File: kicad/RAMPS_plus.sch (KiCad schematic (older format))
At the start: 20 parts, among them CON1 CON10, CON2 CON8, CON3 CON8, CON4 CON8, CON5 CON6, CON6 CON8, CON7 CON8, CON8 CON18x2

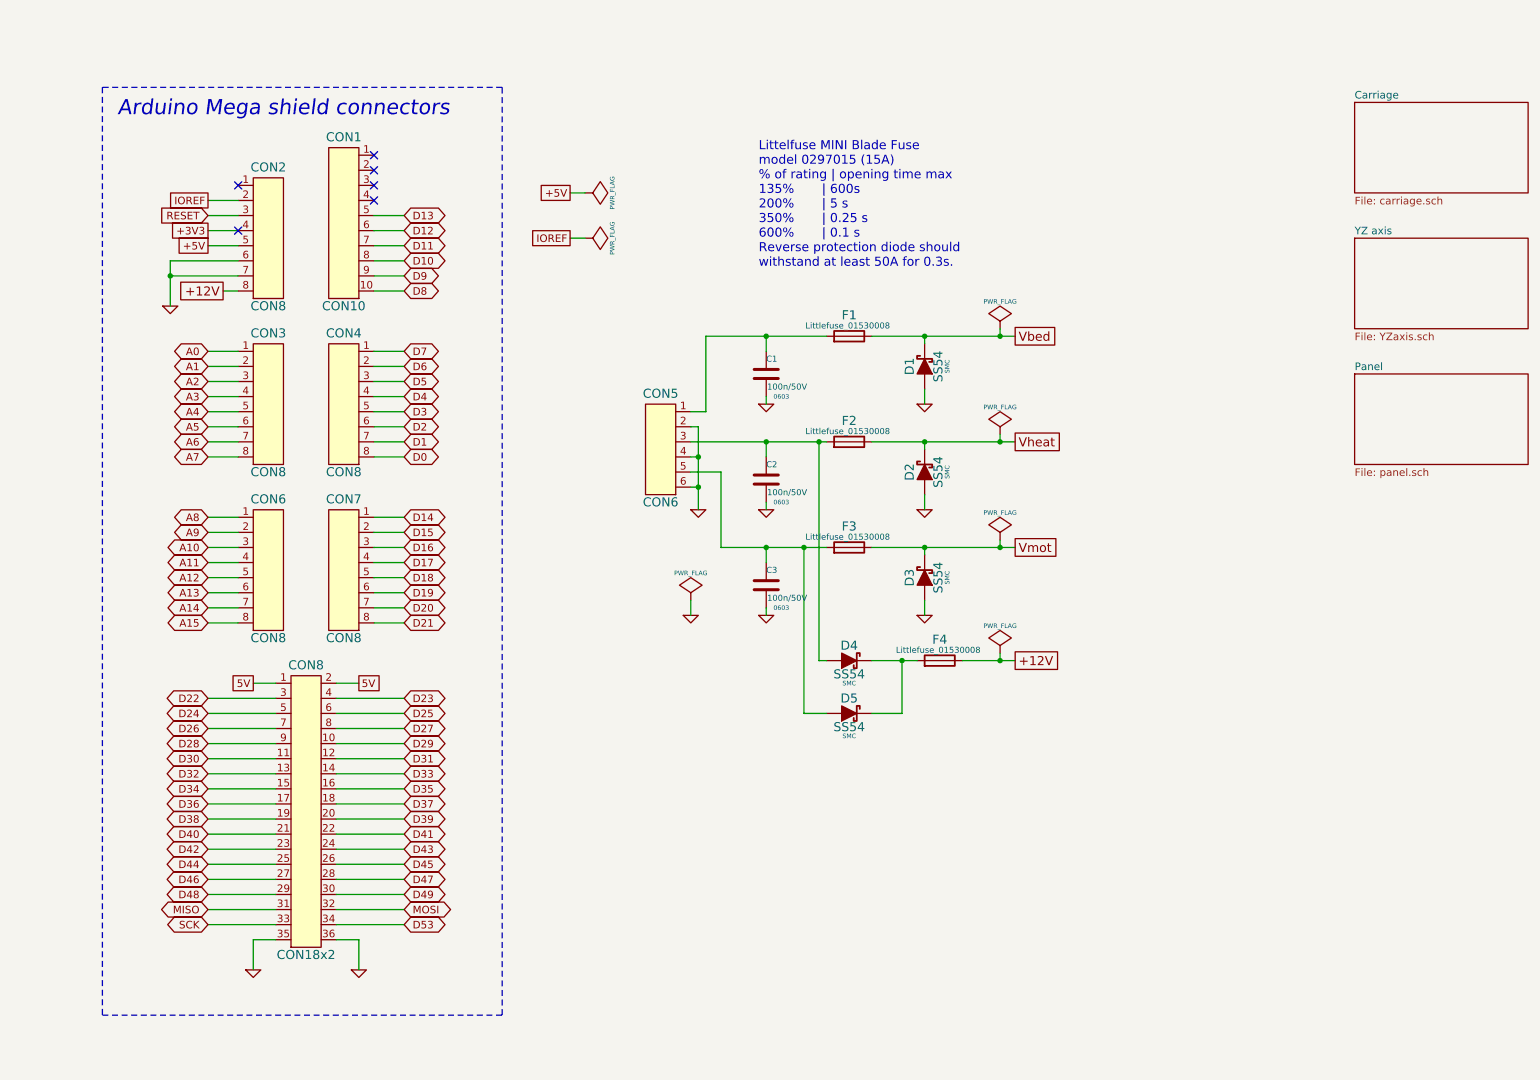
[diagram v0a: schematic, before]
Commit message: Change ULN2803 to discrete MOSFET's FDC6401N
Close #7
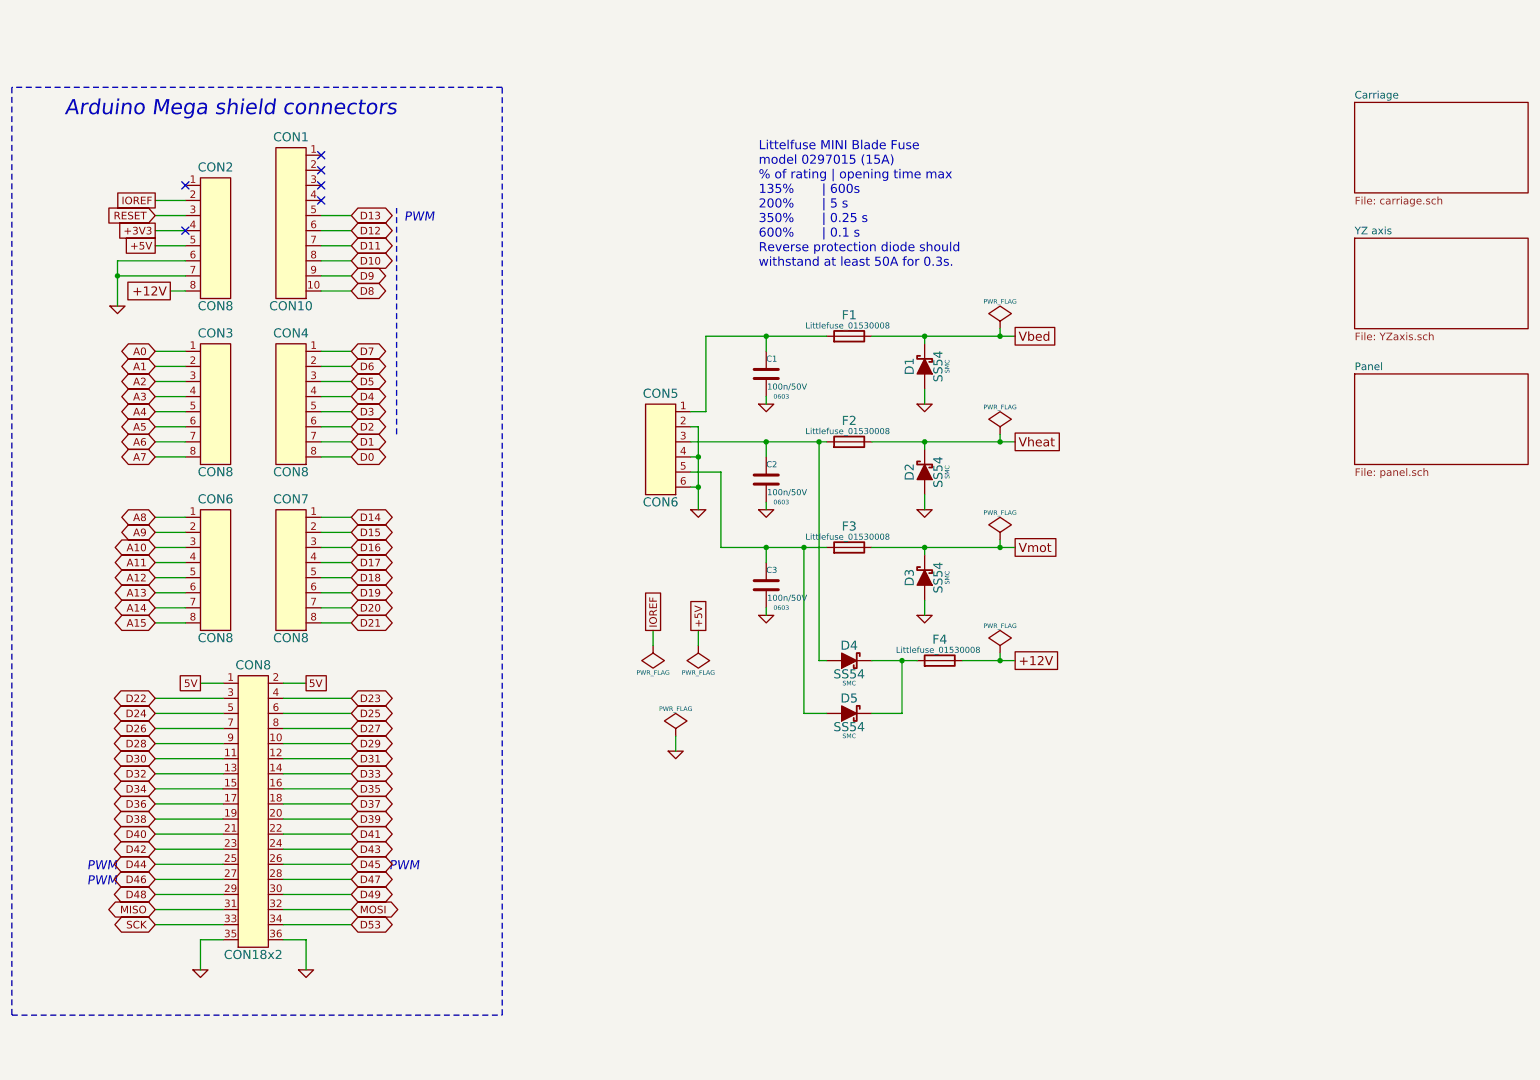
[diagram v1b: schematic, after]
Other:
- note added: "PWM"
- moved on the sheet: CON1, CON2, CON3, CON4, CON6, CON7, CON8

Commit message: Extract power supply circuits to another sheet. Add power off circuit.
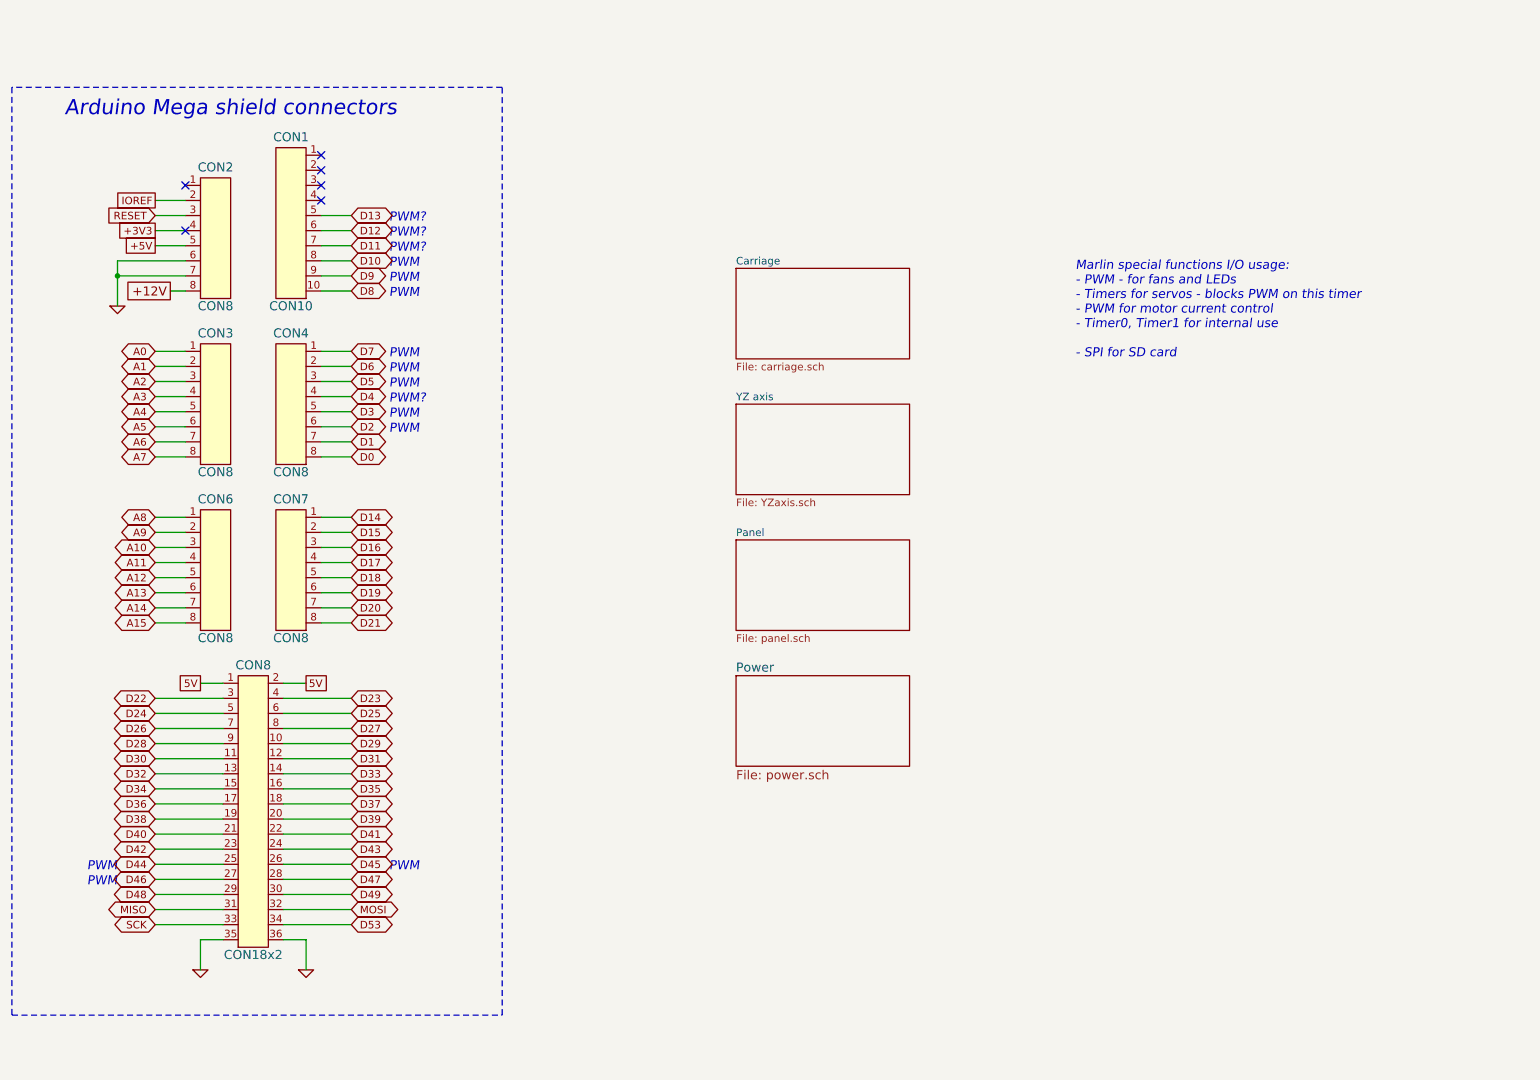
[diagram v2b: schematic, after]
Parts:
- removed C1, C2, C3: 100n/50V, 0603, symbol C
- removed CON5: CON6, symbol CON6
- removed D1, D2, D3, D4, D5: SS54, SMC, symbol SS54
- removed F1, F2, F3, F4: MINI_Blade_Fuse_Holder, Littlefuse_01530008, symbol MINI_Blade_Fuse_Holder
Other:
- note added: "Marlin special functions I/O usage:\n- PWM - for fans and LEDs\n- Timers for servos - blocks PWM on this timer\n- PWM for motor current control\n- Timer0, Timer1 for internal use\n\n- SPI for SD card"
- note added: "PWM?"
- note removed: "Littelfuse MINI Blade Fuse\nmodel 0297015 (15A)\n% of rating | opening time max\n135% | 600s\n200% | 5 s \n350% | 0.25 s \n600% | 0.1 s\nReverse protection diode should \nwithstand at least 50A for 0.3s."

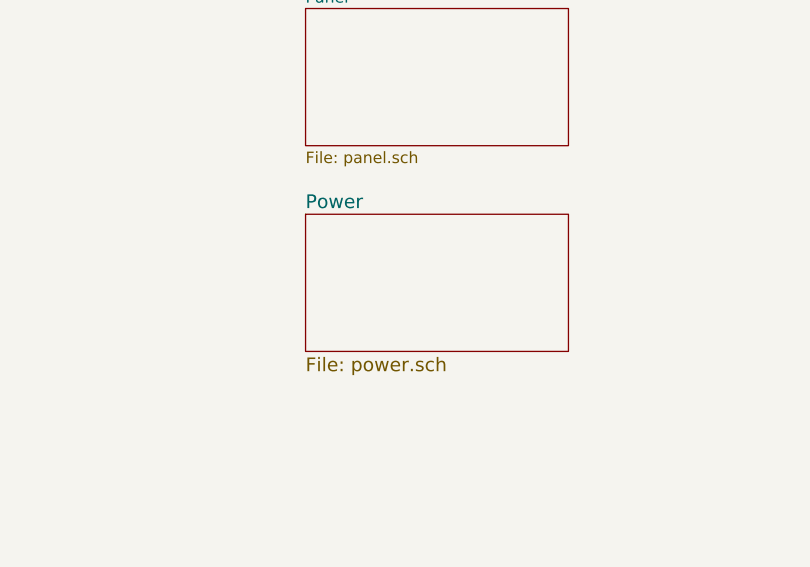
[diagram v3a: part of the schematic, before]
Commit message: Added fan connectors for electronics and power supply
close #15
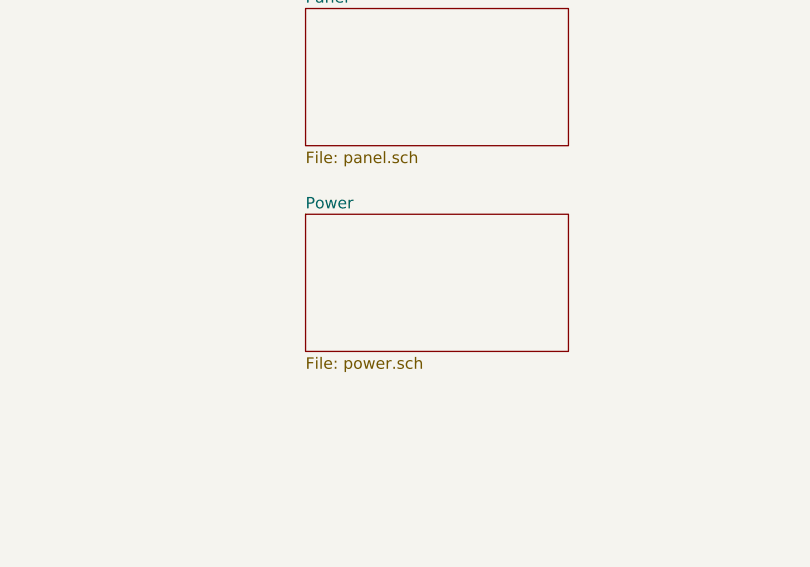
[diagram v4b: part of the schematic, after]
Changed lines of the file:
@@
 $EndComp
 $Comp
-L GND #PWR1
+L GND #PWR01
 U 1 1 536FA4F6
 P 1300 2500
-F 0 "#PWR1" H 1300 2500 30  0001 C CNN
+F 0 "#PWR01" H 1300 2500 30  0001 C CNN
 F 1 "GND" H 1300 2430 30  0001 C CNN
 F 2 "" H 1300 2500 60  0000 C CNN
@@
 $EndComp
 $Comp
-L GND #PWR3
+L GND #PWR02
 U 1 1 536FA739
 P 2550 6900
-F 0 "#PWR3" H 2550 6900 30  0001 C CNN
+F 0 "#PWR02" H 2550 6900 30  0001 C CNN
 F 1 "GND" H 2550 6830 30  0001 C CNN
 F 2 "" H 2550 6900 60  0000 C CNN
@@
 $EndComp
 $Comp
-L GND #PWR2
+L GND #PWR03
 U 1 1 536FA866
 P 1850 6900
-F 0 "#PWR2" H 1850 6900 30  0001 C CNN
+F 0 "#PWR03" H 1850 6900 30  0001 C CNN
 F 1 "GND" H 1850 6830 30  0001 C CNN
 F 2 "" H 1850 6900 60  0000 C CNN
@@
 S 5400 4950 1150 600
 U 539431DE
-F0 "Power" 60
-F1 "power.sch" 60
+F0 "Power" 50
+F1 "power.sch" 50
 $EndSheet
 $EndSCHEMATC

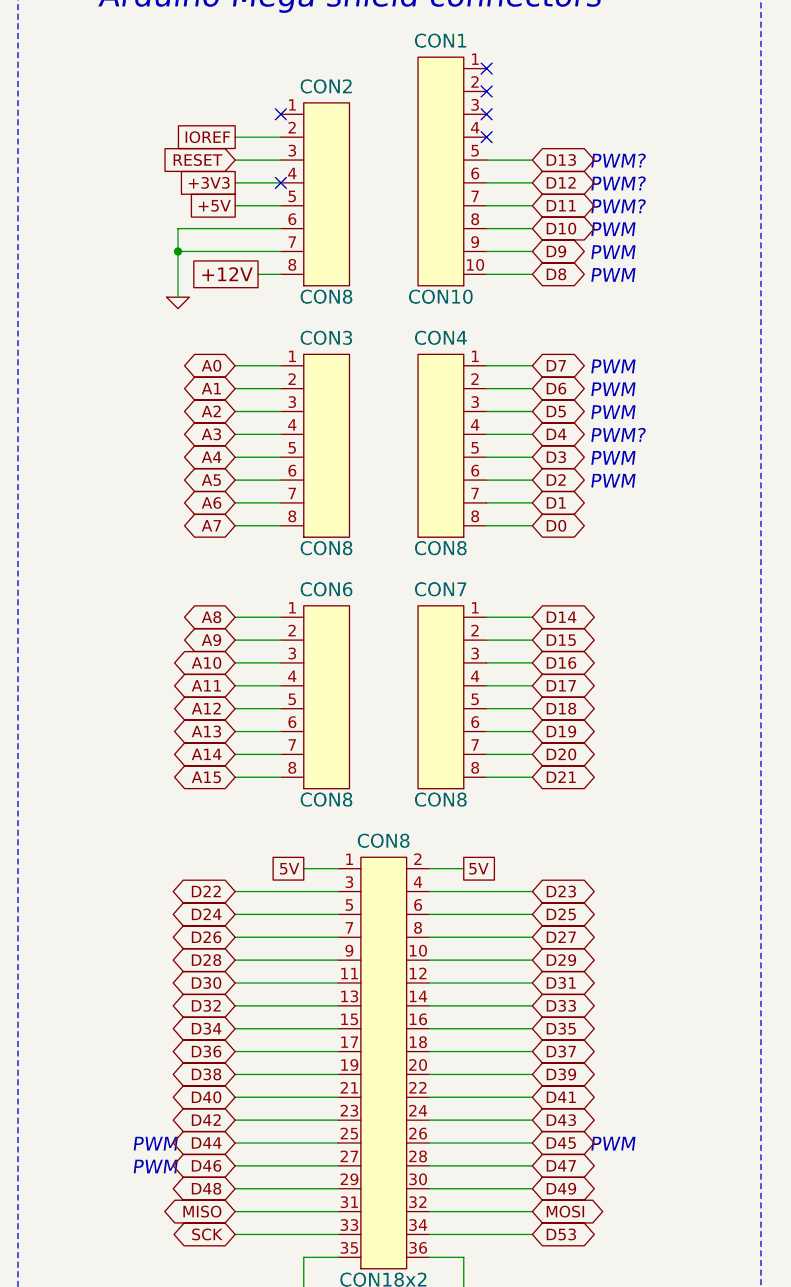
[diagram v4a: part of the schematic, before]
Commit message: Add footprint informations
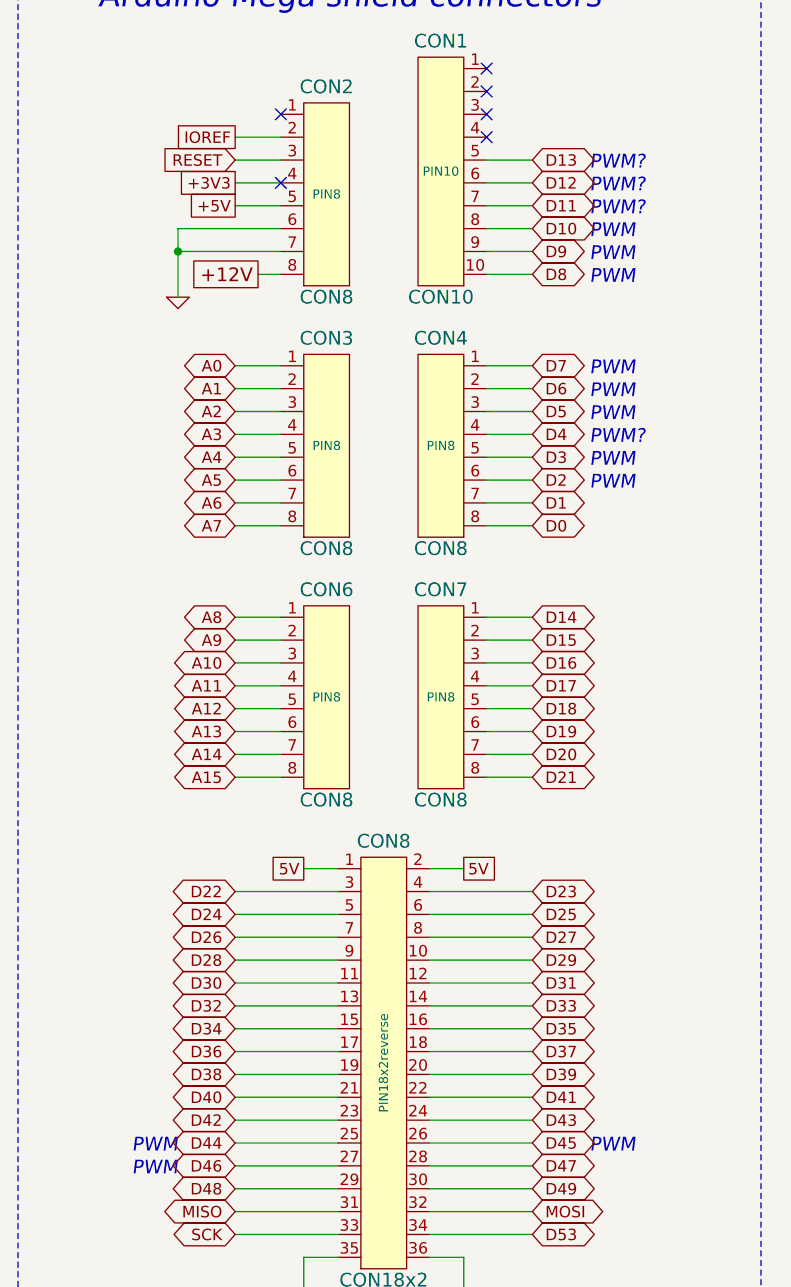
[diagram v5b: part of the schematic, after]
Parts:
- CON1: footprint (none) -> PIN10
- CON2, CON3, CON4, CON6, CON7: footprint (none) -> PIN8
- CON8: footprint (none) -> PIN18x2reverse
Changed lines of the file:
@@
 F 0 "CON2" H 1950 2520 60  0000 C CNN
 F 1 "CON8" H 1950 1600 60  0000 C CNN
-F 2 "" H 1950 2050 40  0000 C CNN
+F 2 "PIN8" H 1950 2050 40  0000 C CNN
 F 3 "" H 1950 2050 40  0000 C CNN
 	1    1950 2050
@@
 F 0 "CON3" H 1950 3620 60  0000 C CNN
 F 1 "CON8" H 1950 2700 60  0000 C CNN
-F 2 "" H 1950 3150 40  0000 C CNN
+F 2 "PIN8" H 1950 3150 40  0000 C CNN
 F 3 "" H 1950 3150 40  0000 C CNN
 	1    1950 3150
@@
 F 0 "CON6" H 1950 4720 60  0000 C CNN
 F 1 "CON8" H 1950 3800 60  0000 C CNN
-F 2 "" H 1950 4250 40  0000 C CNN
+F 2 "PIN8" H 1950 4250 40  0000 C CNN
 F 3 "" H 1950 4250 40  0000 C CNN
 	1    1950 4250
@@
 F 0 "CON7" H 2450 4720 60  0000 C CNN
 F 1 "CON8" H 2450 3800 60  0000 C CNN
-F 2 "" H 2450 4250 40  0000 C CNN
+F 2 "PIN8" H 2450 4250 40  0000 C CNN
 F 3 "" H 2450 4250 40  0000 C CNN
 	1    2450 4250
@@
 F 0 "CON4" H 2450 3620 60  0000 C CNN
 F 1 "CON8" H 2450 2700 60  0000 C CNN
-F 2 "" H 2450 3150 40  0000 C CNN
+F 2 "PIN8" H 2450 3150 40  0000 C CNN
 F 3 "" H 2450 3150 40  0000 C CNN
 	1    2450 3150
@@
 F 0 "CON1" H 2450 2520 60  0000 C CNN
 F 1 "CON10" H 2450 1400 60  0000 C CNN
-F 2 "" H 2450 1950 40  0000 C CNN
+F 2 "PIN10" H 2450 1950 40  0000 C CNN
 F 3 "" H 2450 1950 40  0000 C CNN
 	1    2450 1950
@@
 F 0 "CON8" H 2200 6820 60  0000 C CNN
 F 1 "CON18x2" H 2200 4900 60  0000 C CNN
-F 2 "" H 2200 5850 40  0000 C CNN
+F 2 "PIN18x2reverse" V 2200 5850 40  0000 C CNN
 F 3 "" H 2200 5850 40  0000 C CNN
 	1    2200 5850

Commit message: Place arduino shield connectors
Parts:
- added MECH?: ArduinoMegaShield, symbol ArduinoMegaShield
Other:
- moved on the sheet: CON1, CON2, CON3, CON4, CON6, CON7, CON8
